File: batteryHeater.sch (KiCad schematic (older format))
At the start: 27 parts

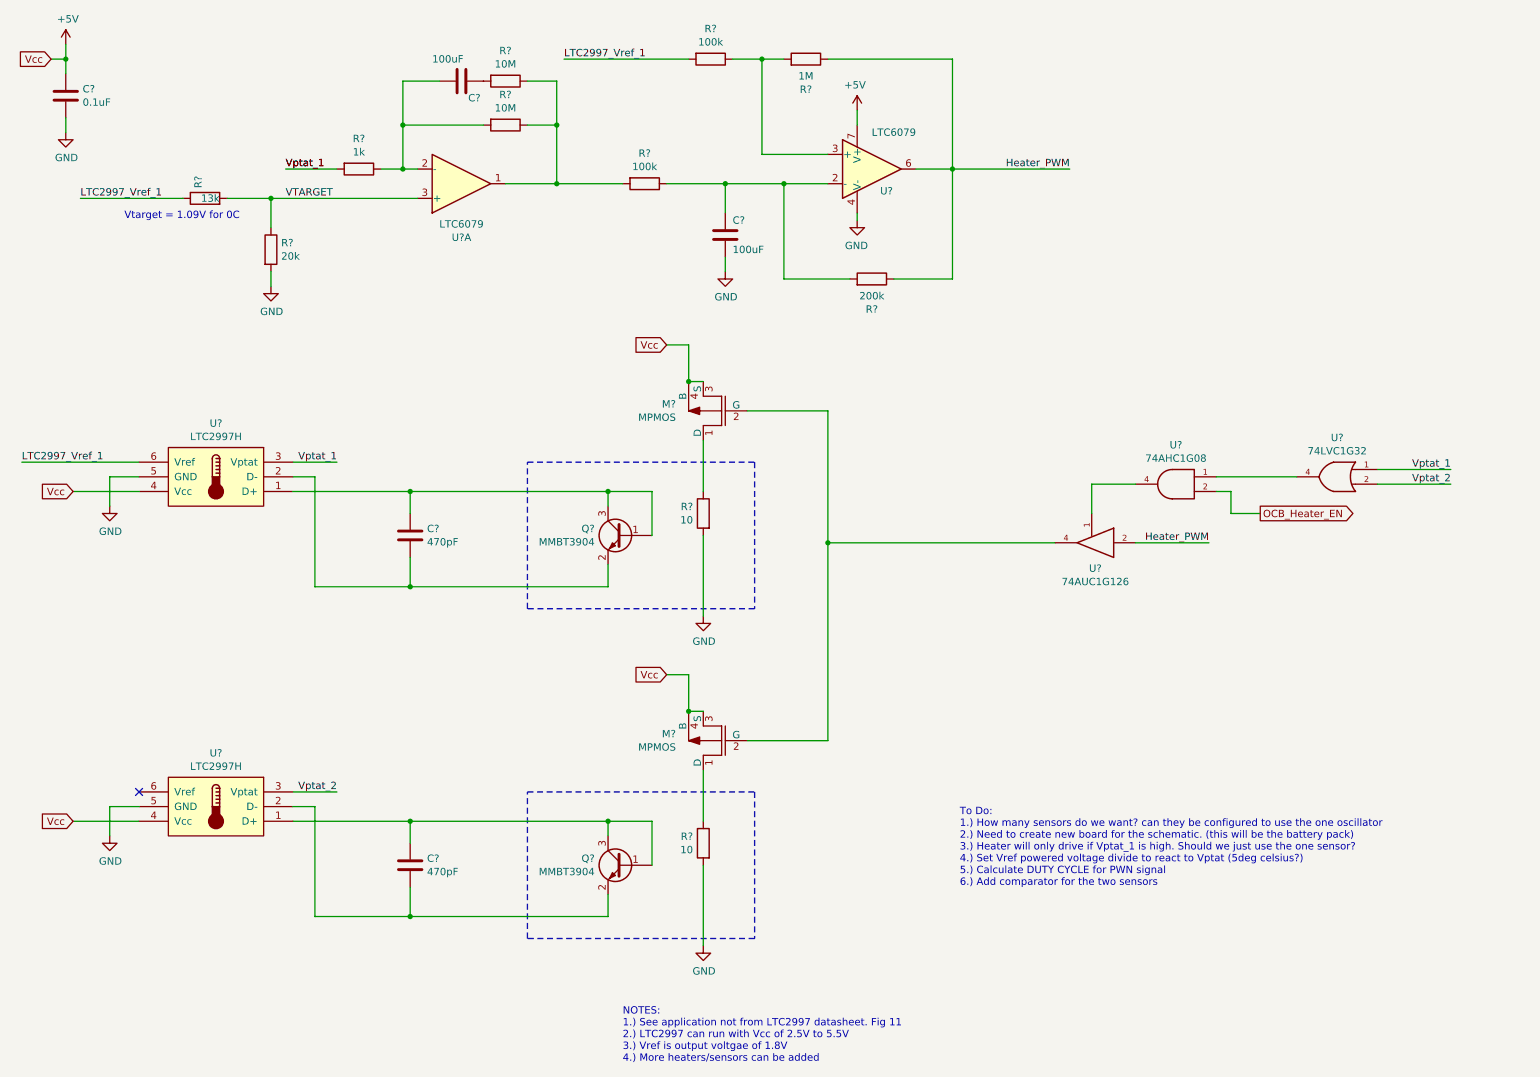
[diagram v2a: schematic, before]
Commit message: added burn wire load switches
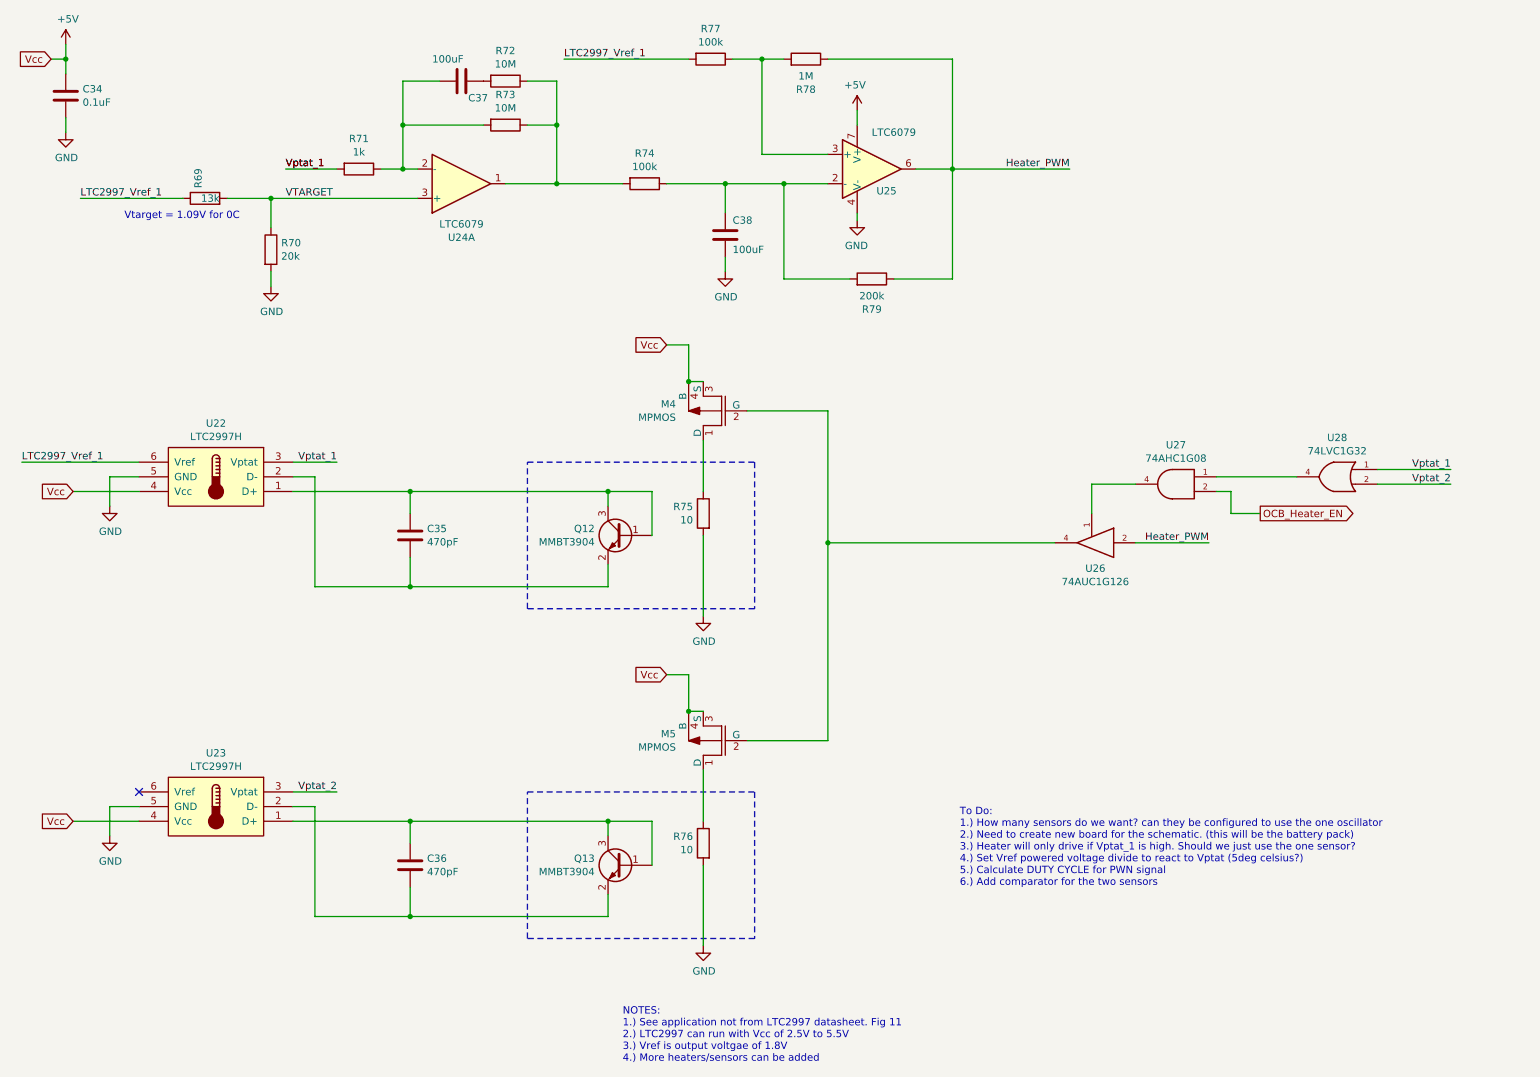
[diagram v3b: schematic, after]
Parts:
- gave numbers to parts that had none: 27
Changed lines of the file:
@@
 $EndComp
 $Comp
-L Main-rescue:C-Device C?
+L Main-rescue:C-Device C34
 U 1 1 5D1F3804
 P 900 1100
-F 0 "C?" H 1015 1146 50  0000 L CNN
+F 0 "C34" H 1015 1146 50  0000 L CNN
 F 1 "0.1uF" H 1015 1055 50  0000 L CNN
 F 2 "Capacitors_SMD:C_0805_HandSoldering" H 938 950 50  0001 C CNN
@@
 	3250 3800 3250 3950
 $Comp
-L Main-rescue:C-Device C?
+L Main-rescue:C-Device C35
 U 1 1 5D1F5549
 P 3250 4100
-F 0 "C?" H 3365 4146 50  0000 L CNN
+F 0 "C35" H 3365 4146 50  0000 L CNN
 F 1 "470pF" H 3365 4055 50  0000 L CNN
 F 2 "Capacitors_SMD:C_0805_HandSoldering" H 3288 3950 50  0001 C CNN
@@
 Connection ~ 4600 3800
 $Comp
-L Main-rescue:R-Device R?
+L Main-rescue:R-Device R69
 U 1 1 5D1F18BB
 P 1850 1800
-F 0 "R?" H 1920 1846 50  0000 L CNN
+F 0 "R69" H 1920 1846 50  0000 L CNN
 F 1 "13k" V 1850 1700 50  0000 L CNN
 F 2 "Resistors_SMD:R_0805_HandSoldering" V 1780 1800 50  0001 C CNN
@@
 $EndComp
 $Comp
-L Main-rescue:R-Device R?
+L Main-rescue:R-Device R70
 U 1 1 5D1F1951
 P 2300 2150
-F 0 "R?" H 2370 2196 50  0000 L CNN
+F 0 "R70" H 2370 2196 50  0000 L CNN
 F 1 "20k" H 2370 2105 50  0000 L CNN
 F 2 "Resistors_SMD:R_0805_HandSoldering" V 2230 2150 50  0001 C CNN
@@
 $EndComp
 $Comp
-L Main-rescue:LT1492-Amplifier_Operational U?
+L Main-rescue:LT1492-Amplifier_Operational U24
 U 1 1 5D1F2936
 P 3600 1700
-F 0 "U?" H 3600 2067 50  0000 C CNN
+F 0 "U24" H 3600 2067 50  0000 C CNN
 F 1 "LTC6079" H 3600 1976 50  0000 C CNN
 F 2 "" H 3600 1700 50  0001 C CNN
@@
 	2300 1800 2300 2000
 $Comp
-L Main-rescue:R-Device R?
+L Main-rescue:R-Device R71
 U 1 1 5D1F6B8A
 P 2900 1600
-F 0 "R?" V 2693 1600 50  0000 C CNN
+F 0 "R71" V 2693 1600 50  0000 C CNN
 F 1 "1k" V 2784 1600 50  0000 C CNN
 F 2 "Resistors_SMD:R_0805_HandSoldering" V 2830 1600 50  0001 C CNN
@@
 $EndComp
 $Comp
-L Main-rescue:C-Device C?
+L Main-rescue:C-Device C37
 U 1 1 5D1F894B
 P 3600 1000
-F 0 "C?" V 3715 1046 50  0000 L CNN
+F 0 "C37" V 3715 1046 50  0000 L CNN
 F 1 "100uF" V 3450 800 50  0000 L CNN
 F 2 "Capacitors_SMD:C_0805_HandSoldering" H 3638 850 50  0001 C CNN
@@
 $EndComp
 $Comp
-L Main-rescue:R-Device R?
+L Main-rescue:R-Device R72
 U 1 1 5D1F89EA
 P 3900 1000
-F 0 "R?" V 3693 1000 50  0000 C CNN
+F 0 "R72" V 3693 1000 50  0000 C CNN
 F 1 "10M" V 3784 1000 50  0000 C CNN
 F 2 "Resistors_SMD:R_0805_HandSoldering" V 3830 1000 50  0001 C CNN
@@
 $EndComp
 $Comp
-L Main-rescue:R-Device R?
+L Main-rescue:R-Device R73
 U 1 1 5D1F8A1E
 P 3900 1300
-F 0 "R?" V 3693 1300 50  0000 C CNN
+F 0 "R73" V 3693 1300 50  0000 C CNN
 F 1 "10M" V 3784 1300 50  0000 C CNN
 F 2 "Resistors_SMD:R_0805_HandSoldering" V 3830 1300 50  0001 C CNN
@@
 	4050 1300 4250 1300
 $Comp
-L Main-rescue:R-Device R?
+L Main-rescue:R-Device R74
 U 1 1 5D1FAB9D
 P 4850 1700
-F 0 "R?" V 4643 1700 50  0000 C CNN
+F 0 "R74" V 4643 1700 50  0000 C CNN
 F 1 "100k" V 4734 1700 50  0000 C CNN
 F 2 "Resistors_SMD:R_0805_HandSoldering" V 4780 1700 50  0001 C CNN
@@
 	4250 1700 4700 1700
 $Comp
-L Main-rescue:LM6171D-Amplifier_Operational U?
+L Main-rescue:LM6171D-Amplifier_Operational U25
 U 1 1 5D1F6AA8
 P 6400 1600
-F 0 "U?" H 6500 1450 50  0000 C CNN
+F 0 "U25" H 6500 1450 50  0000 C CNN
 F 1 "LTC6079" H 6550 1850 50  0000 C CNN
 F 2 "Package_SO:SOIC-8_3.9x4.9mm_P1.27mm" H 6300 1400 50  0001 L CNN
@@
 	6950 850  6100 850
 $Comp
-L Main-rescue:R-Device R?
+L Main-rescue:R-Device R78
 U 1 1 5D1FBD9D
 P 5950 850
-F 0 "R?" V 5743 850 50  0000 C CNN
+F 0 "R78" V 5743 850 50  0000 C CNN
 F 1 "1M" V 5834 850 50  0000 C CNN
 F 2 "Resistors_SMD:R_0805_HandSoldering" V 5880 850 50  0001 C CNN
@@
 Vcc
 $Comp
-L Main-rescue:R-Device R?
+L Main-rescue:R-Device R75
 U 1 1 5D211CC9
 P 5250 3950
-F 0 "R?" H 5320 3996 50  0000 L CNN
+F 0 "R75" H 5320 3996 50  0000 L CNN
 F 1 "10" H 5320 3905 50  0000 L CNN
 F 2 "Resistors_THT:R_Bare_Metal_Element_L12.4mm_W4.8mm_P11.40mm" V 5180 3950 50  0001 C CNN
@@
 $EndComp
 $Comp
-L Main-rescue:MPMOS-pspice M?
+L Main-rescue:MPMOS-pspice M4
 U 1 1 5D21272A
 P 5350 3250
-F 0 "M?" H 5637 3296 50  0000 L CNN
+F 0 "M4" H 5637 3296 50  0000 L CNN
 F 1 "MPMOS" H 5637 3205 50  0000 L CNN
 F 2 "Housings_SSOP:MSOP-8-1EP_3x3mm_Pitch0.65mm" H 5350 3250 50  0001 C CNN
@@
 P 1900 3450
 AR Path="/5E4295DF" Ref="U?"  Part="1"
-AR Path="/5D20C8DB/5E4295DF" Ref="U?"  Part="1"
-F 0 "U?" H 1875 3565 50  0000 C CNN
+AR Path="/5D20C8DB/5E4295DF" Ref="U22"  Part="1"
+F 0 "U22" H 1875 3565 50  0000 C CNN
 F 1 "LTC2997H" H 1875 3474 50  0000 C CNN
 F 2 "" H 1900 3450 50  0001 C CNN
@@
 Connection ~ 6950 1600
 $Comp
-L Main-rescue:R-Device R?
+L Main-rescue:R-Device R77
 U 1 1 5E4B7B53
 P 5300 850
-F 0 "R?" V 5093 850 50  0000 C CNN
+F 0 "R77" V 5093 850 50  0000 C CNN
 F 1 "100k" V 5184 850 50  0000 C CNN
 F 2 "Resistors_SMD:R_0805_HandSoldering" V 5230 850 50  0001 C CNN
@@
 Connection ~ 3250 4450
 $Comp
-L Main-rescue:R-Device R?
+L Main-rescue:R-Device R79
 U 1 1 5D1FCAF1
 P 6400 2350
-F 0 "R?" V 6193 2350 50  0000 C CNN
+F 0 "R79" V 6193 2350 50  0000 C CNN
 F 1 "200k" V 6284 2350 50  0000 C CNN
 F 2 "Resistors_SMD:R_0805_HandSoldering" V 6330 2350 50  0001 C CNN
@@
 	5400 1900 5400 1700
 $Comp
-L Main-rescue:C-Device C?
+L Main-rescue:C-Device C38
 U 1 1 5E50ACB0
 P 5400 2050
-F 0 "C?" H 5450 2150 50  0000 L CNN
+F 0 "C38" H 5450 2150 50  0000 L CNN
 F 1 "100uF" H 5450 1950 50  0000 L CNN
 F 2 "Capacitors_SMD:C_0805_HandSoldering" H 5438 1900 50  0001 C CNN
@@
 	3250 6050 3250 6200
 $Comp
-L Main-rescue:C-Device C?
+L Main-rescue:C-Device C36
 U 1 1 5E560E15
 P 3250 6350
-F 0 "C?" H 3365 6396 50  0000 L CNN
+F 0 "C36" H 3365 6396 50  0000 L CNN
 F 1 "470pF" H 3365 6305 50  0000 L CNN
 F 2 "Capacitors_SMD:C_0805_HandSoldering" H 3288 6200 50  0001 C CNN
@@
 	950  6050 1400 6050
 $Comp
-L Main-rescue:R-Device R?
+L Main-rescue:R-Device R76
 U 1 1 5E560E2B
 P 5250 6200
-F 0 "R?" H 5320 6246 50  0000 L CNN
+F 0 "R76" H 5320 6246 50  0000 L CNN
 F 1 "10" H 5320 6155 50  0000 L CNN
 F 2 "Resistors_THT:R_Bare_Metal_Element_L12.4mm_W4.8mm_P11.40mm" V 5180 6200 50  0001 C CNN
@@
 $EndComp
 $Comp
-L Main-rescue:MPMOS-pspice M?
+L Main-rescue:MPMOS-pspice M5
 U 1 1 5E560E31
 P 5350 5500
-F 0 "M?" H 5637 5546 50  0000 L CNN
+F 0 "M5" H 5637 5546 50  0000 L CNN
 F 1 "MPMOS" H 5637 5455 50  0000 L CNN
 F 2 "Housings_SSOP:MSOP-8-1EP_3x3mm_Pitch0.65mm" H 5350 5500 50  0001 C CNN
@@
 P 1900 5700
 AR Path="/5E560E42" Ref="U?"  Part="1"
-AR Path="/5D20C8DB/5E560E42" Ref="U?"  Part="1"
-F 0 "U?" H 1875 5815 50  0000 C CNN
+AR Path="/5D20C8DB/5E560E42" Ref="U23"  Part="1"
+F 0 "U23" H 1875 5815 50  0000 C CNN
 F 1 "LTC2997H" H 1875 5724 50  0000 C CNN
 F 2 "" H 1900 5700 50  0001 C CNN
@@
 	5150 5050 5000 5050
 $Comp
-L 74xGxx:74LVC1G32 U?
+L 74xGxx:74LVC1G32 U28
 U 1 1 5E56CF68
 P 9550 3700
-F 0 "U?" H 9525 3967 50  0000 C CNN
+F 0 "U28" H 9525 3967 50  0000 C CNN
 F 1 "74LVC1G32" H 9525 3876 50  0000 C CNN
 F 2 "" H 9550 3700 50  0001 C CNN
@@
 $EndComp
 $Comp
-L 74xGxx:74AHC1G08 U?
+L 74xGxx:74AHC1G08 U27
 U 1 1 5E56DEF1
 P 8450 3750
-F 0 "U?" H 8425 4017 50  0000 C CNN
+F 0 "U27" H 8425 4017 50  0000 C CNN
 F 1 "74AHC1G08" H 8425 3926 50  0000 C CNN
 F 2 "" H 8450 3750 50  0001 C CNN
@@
 NoConn ~ 1400 5850
 $Comp
-L Transistor_BJT:MMBT3904 Q?
+L Transistor_BJT:MMBT3904 Q13
 U 1 1 5E3D63BD
 P 4700 6350
-F 0 "Q?" H 4891 6396 50  0000 L CNN
+F 0 "Q13" H 4891 6396 50  0000 L CNN
 F 1 "MMBT3904" H 4891 6305 50  0000 L CNN
 F 2 "Package_TO_SOT_SMD:SOT-23" H 4900 6275 50  0001 L CIN
@@
 $EndComp
 $Comp
-L Transistor_BJT:MMBT3904 Q?
+L Transistor_BJT:MMBT3904 Q12
 U 1 1 5E3E16A3
 P 4700 4100
-F 0 "Q?" H 4891 4146 50  0000 L CNN
+F 0 "Q12" H 4891 4146 50  0000 L CNN
 F 1 "MMBT3904" H 4891 4055 50  0000 L CNN
 F 2 "Package_TO_SOT_SMD:SOT-23" H 4900 4025 50  0001 L CIN
@@
 	9300 3700 8750 3700
 $Comp
-L 74xGxx:74AUC1G126 U?
+L 74xGxx:74AUC1G126 U26
 U 1 1 5E3EB5FA
 P 7900 4150
-F 0 "U?" H 7875 3975 50  0000 C CNN
+F 0 "U26" H 7875 3975 50  0000 C CNN
 F 1 "74AUC1G126" H 7875 3884 50  0000 C CNN
 F 2 "" H 7900 4150 50  0001 C CNN
